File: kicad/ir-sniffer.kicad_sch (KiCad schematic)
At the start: 6 parts, among them U1 NodeMCU_1.0_(ESP-12E), U2 VS1838B

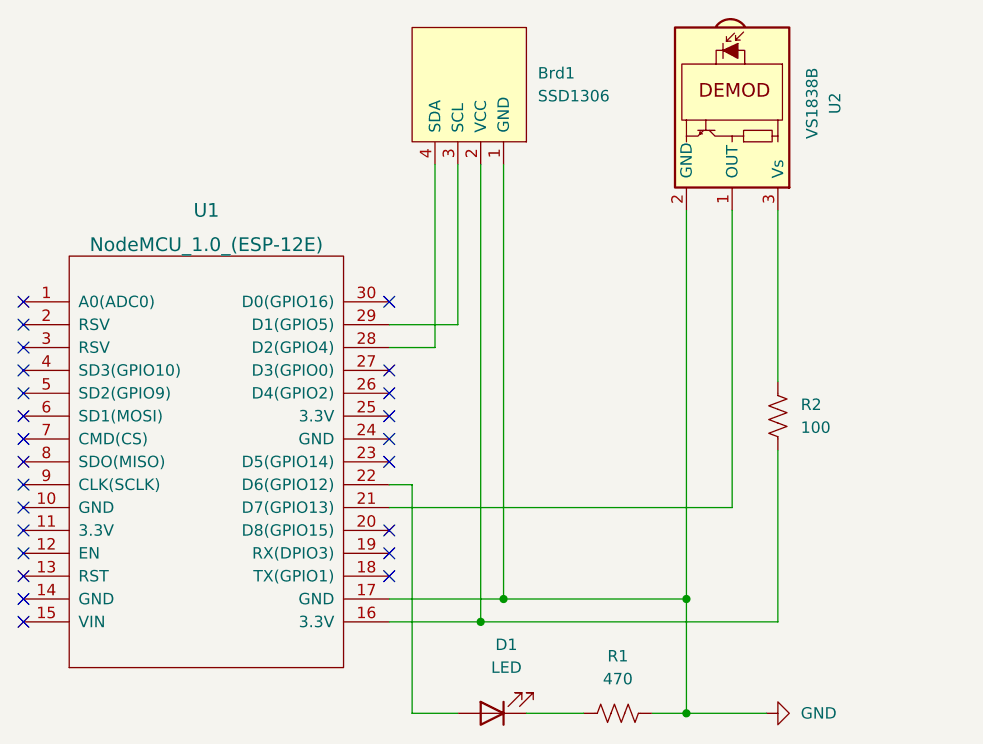
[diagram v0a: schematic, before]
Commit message: add oscilloscope debug headers
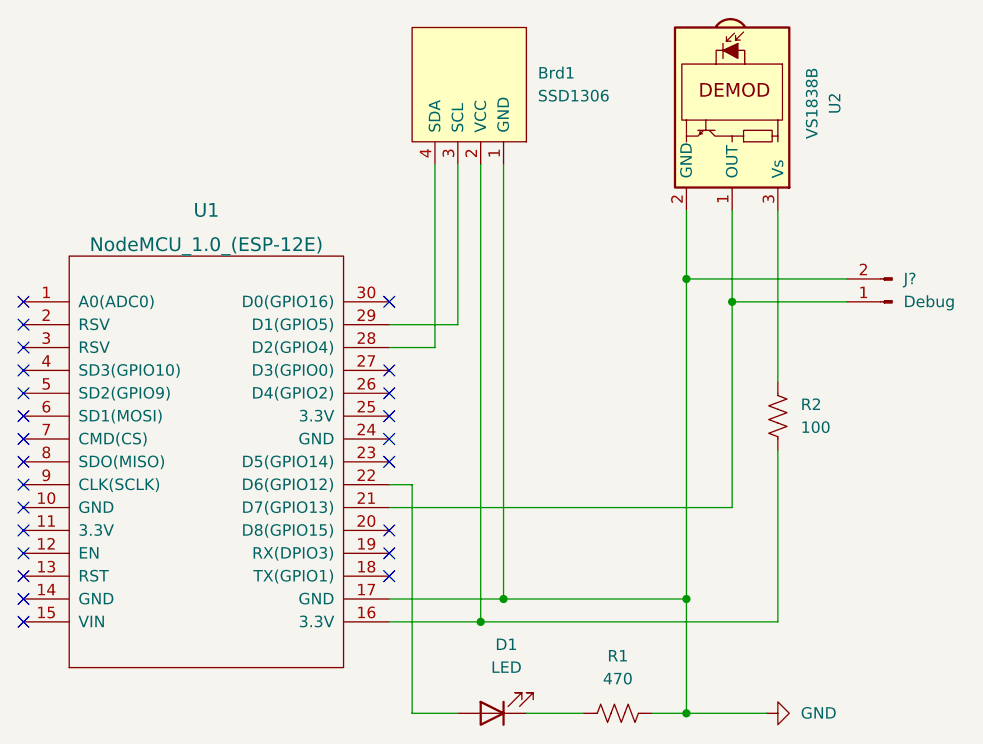
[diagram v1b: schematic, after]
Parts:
- added J?: Debug, symbol Connector:Conn_01x02_Male
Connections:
- net GND: now also J?.2 (Pin_2)
- net at U1.21 (D7(GPIO13)), U2.1 (OUT): now also J?.1 (Pin_1)
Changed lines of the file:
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@@
   (junction (at 138.43 124.46) (diameter 0) (color 0 0 0 0)
   )
+  (junction (at 166.37 88.9) (diameter 0) (color 0 0 0 0)
+  )
   (junction (at 140.97 121.92) (diameter 0) (color 0 0 0 0)
+  )
+  (junction (at 161.29 86.36) (diameter 0) (color 0 0 0 0)
   )
   (junction (at 161.29 134.62) (diameter 0) (color 0 0 0 0)
@@
     (stroke (width 0) (type default) (color 0 0 0 0))
   )
+  (wire (pts (xy 166.37 88.9) (xy 166.37 78.74))
+    (stroke (width 0) (type default) (color 0 0 0 0))
+  )
   (wire (pts (xy 157.48 134.62) (xy 161.29 134.62))
     (stroke (width 0) (type default) (color 0 0 0 0))
@@
     (stroke (width 0) (type default) (color 0 0 0 0))
   )
-  (wire (pts (xy 161.29 78.74) (xy 161.29 121.92))
+  (wire (pts (xy 161.29 78.74) (xy 161.29 86.36))
+    (stroke (width 0) (type default) (color 0 0 0 0))
+  )
+  (wire (pts (xy 161.29 86.36) (xy 179.07 86.36))
     (stroke (width 0) (type default) (color 0 0 0 0))
   )
@@
     (stroke (width 0) (type default) (color 0 0 0 0))
   )
-  (wire (pts (xy 166.37 111.76) (xy 166.37 78.74))
+  (wire (pts (xy 161.29 86.36) (xy 161.29 121.92))
+    (stroke (width 0) (type default) (color 0 0 0 0))
+  )
+  (wire (pts (xy 166.37 111.76) (xy 166.37 88.9))
     (stroke (width 0) (type default) (color 0 0 0 0))
   )
   (wire (pts (xy 161.29 134.62) (xy 161.29 121.92))
+    (stroke (width 0) (type default) (color 0 0 0 0))
+  )
+  (wire (pts (xy 166.37 88.9) (xy 179.07 88.9))
     (stroke (width 0) (type default) (color 0 0 0 0))
   )
@@
     )
     (property "Datasheet" "~" (id 3) (at 171.45 101.6 0)
+      (effects (font (size 1.27 1.27)) hide)
+    )
+    (pin "1")
+    (pin "2")
+  )
+  (symbol (lib_id "Connector:Conn_01x02_Male") (at 184.15 88.9 180) (unit 1)
+    (in_bom yes) (on_board yes) (fields_autoplaced)
+    (property "Reference" "J?" (id 0) (at 185.42 86.3599 0)
+      (effects (font (size 1.27 1.27)) (justify right))
+    )
+    (property "Value" "Debug" (id 1) (at 185.42 88.8999 0)
+      (effects (font (size 1.27 1.27)) (justify right))
+    )
+    (property "Footprint" "" (id 2) (at 184.15 88.9 0)
+      (effects (font (size 1.27 1.27)) hide)
+    )
+    (property "Datasheet" "~" (id 3) (at 184.15 88.9 0)
       (effects (font (size 1.27 1.27)) hide)
     )
@@
       (reference "D1") (unit 1) (value "LED") (footprint "")
     )
+    (path "/39140c12-aef6-46ed-81a7-2ab0cc79b6b0"
+      (reference "J?") (unit 1) (value "Debug") (footprint "")
+    )
     (path "/28a3c8c0-1771-4dcc-b7eb-86e749f98d71"
